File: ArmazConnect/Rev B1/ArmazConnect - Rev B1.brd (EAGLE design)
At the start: 165 x 74 mm, 45 parts, among them X0 NC3FAAV2, X1 NC3FAAV2, X2 NC3FAAV2, X3 NC3FAAV2, X4 NC5FAV-SW, X5 NC5MAV-SW, X6 NC5FAV-SW, X7 5504F1-09S-02A-03, X8 87832-26

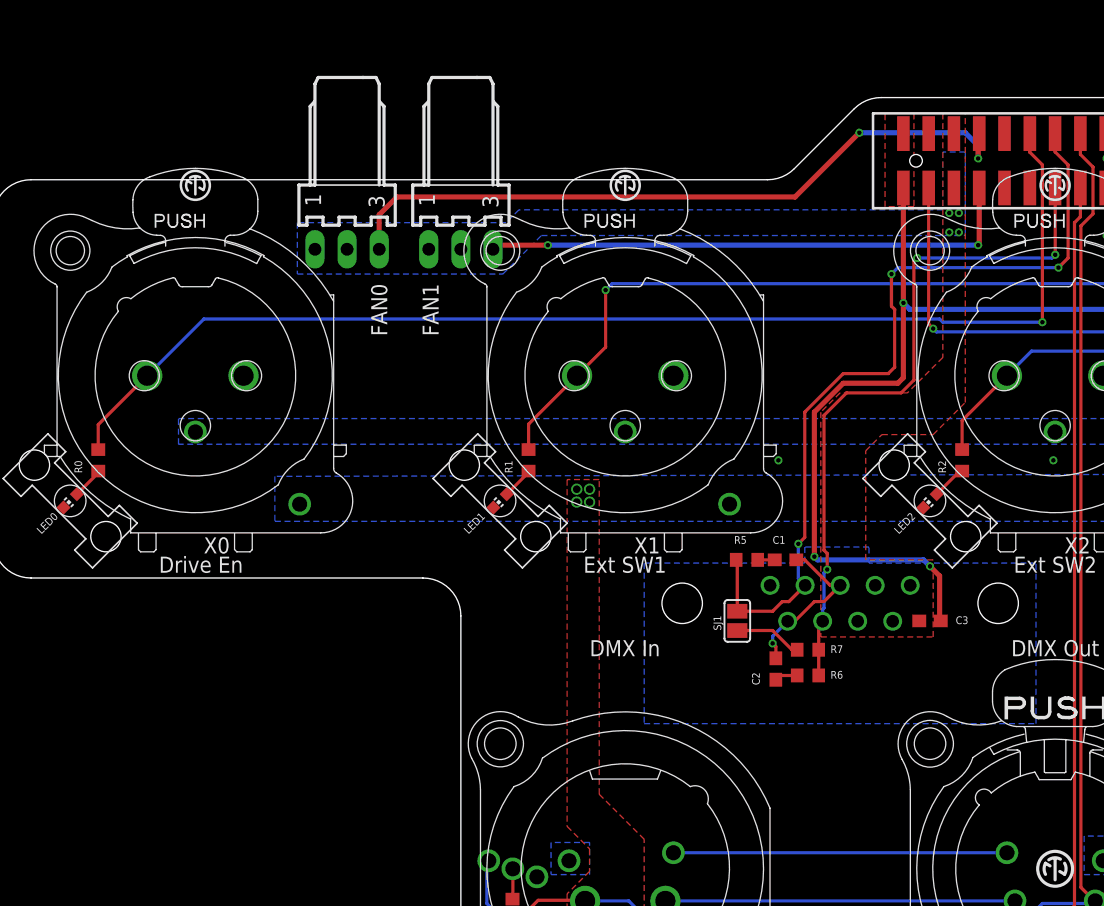
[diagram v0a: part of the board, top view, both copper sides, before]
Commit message: Add 84102C to murata inductance library, add MEE3 to dc/dc converter library, update of ArmazConnect rev B1 (dc/dc 12V to 5V), create Varmo Eagles project
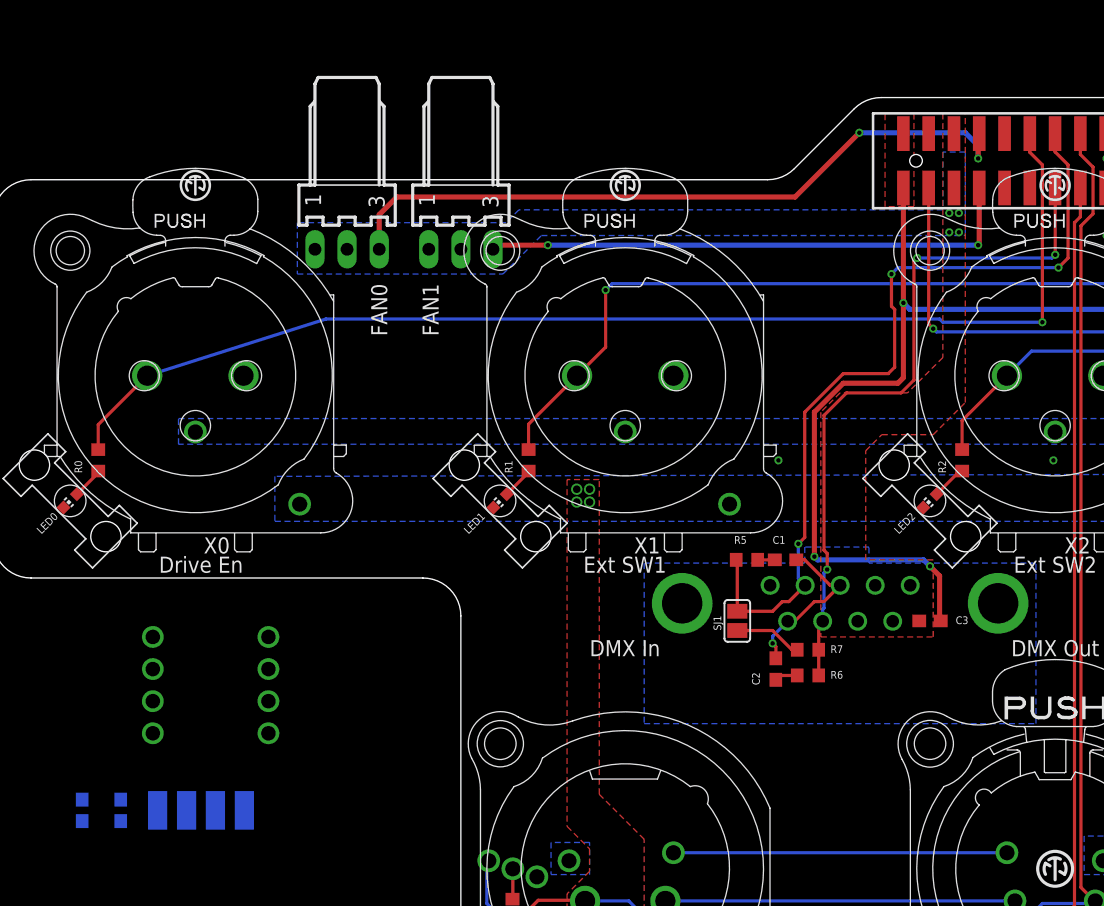
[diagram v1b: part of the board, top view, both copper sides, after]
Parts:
- added C6, C7: 4.7uF, rcl:C0603
- added L1, L2: 10uH, murata-inductance:8200
- added U$1, U$2: MEE3S1205SC, dc-dc-converter:MEE3
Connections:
- new net N$10: L2.1, U$2.4
- new net N$9: L1.1, U$1.4
- net +12V: now also U$1.2, U$2.2
- net +5V: now also C6.1, C7.1, L1.2, L2.2
- net GND: now also C6.2, C7.2, U$1.3, U$2.3
- net GND1: now also U$1.1, U$2.1
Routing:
- net DV0: track 95.5 -> 94.4 mm
